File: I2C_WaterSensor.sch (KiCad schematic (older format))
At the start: 18 parts, among them J1 AVR-ISP-6, J8 Conn_01x07, U2 ATmega328P-AU, Y1 16MHz

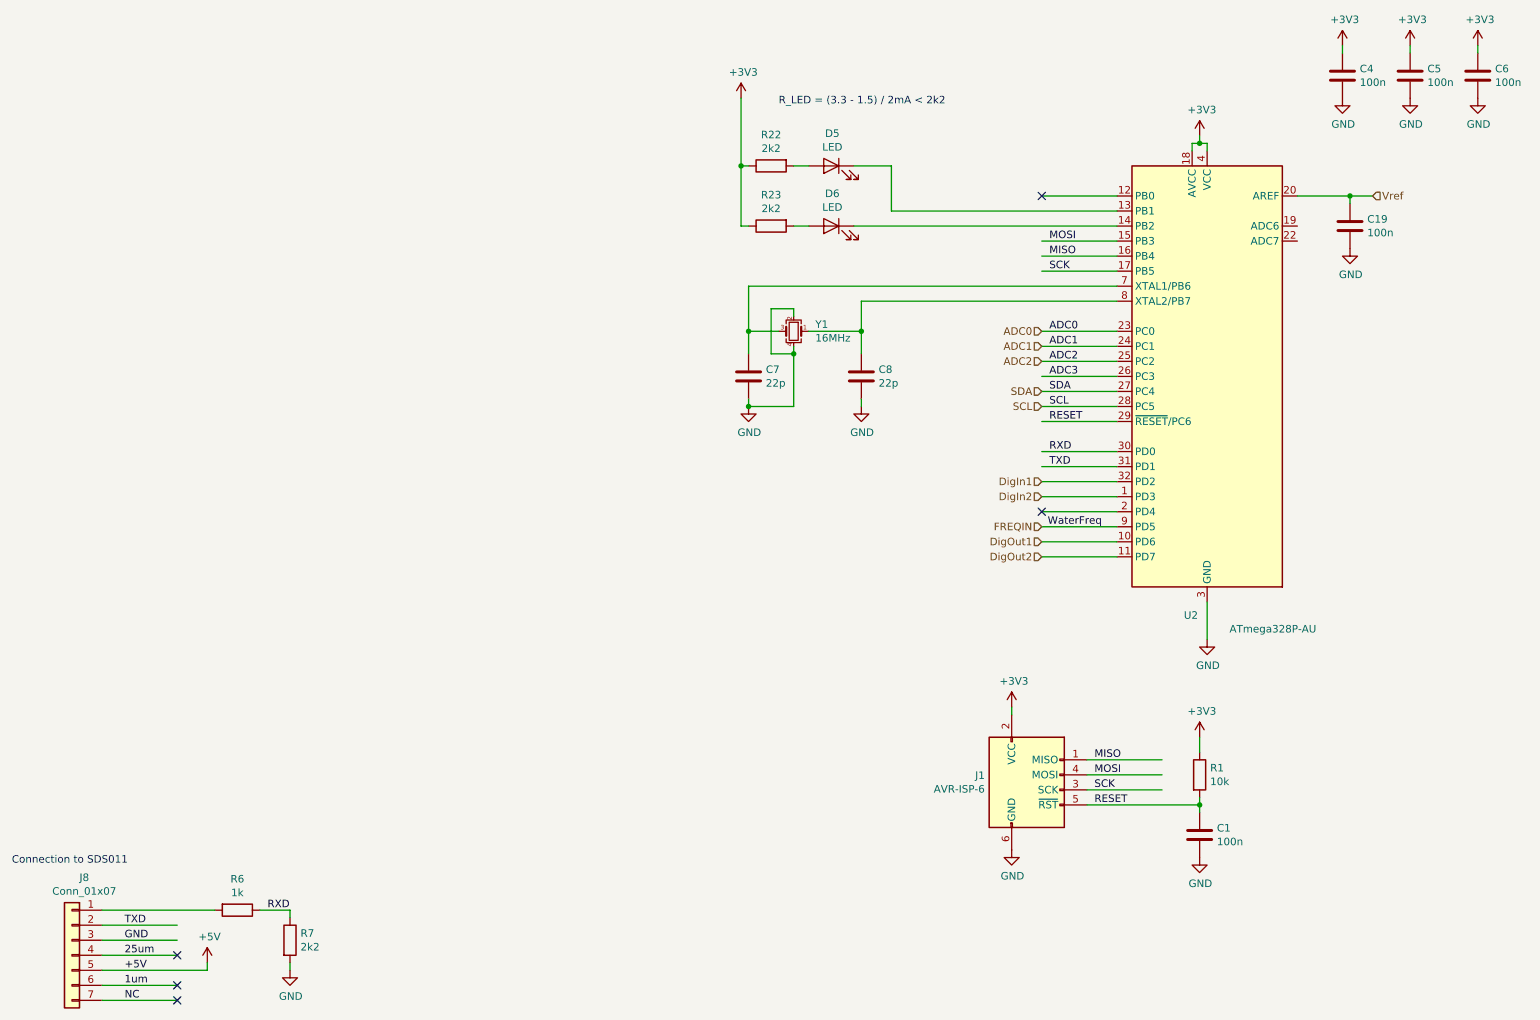
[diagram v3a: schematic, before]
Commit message: included address jumper for AVR, which makes it easier to use multiple of these boards at the same I2C bus.
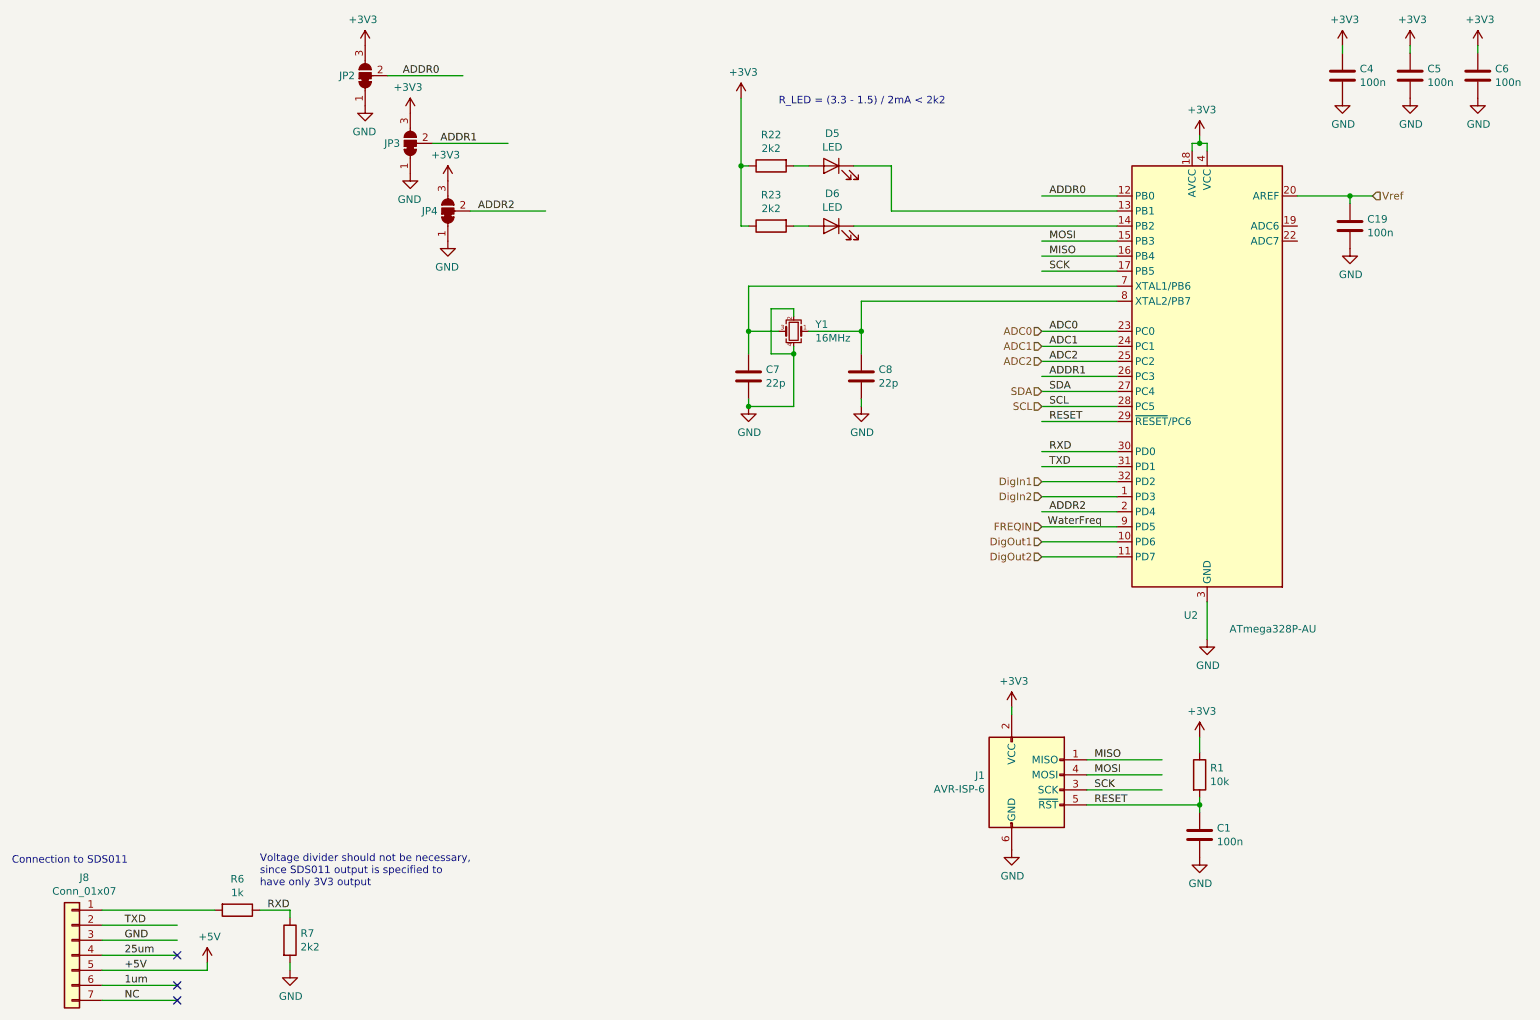
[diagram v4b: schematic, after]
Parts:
- added JP2, JP3, JP4: SolderJumper_3_Bridged12, Jumper:SolderJumper-3_P1.3mm_Bridged12_Pad1.0x1.5mm, symbol Jumper:SolderJumper_3_Bridged12
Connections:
- net labels added: ADDR0, ADDR1, ADDR2
- net labels removed: ADC3
- wire segments 77 -> 80
- no-connect marks 5 -> 3
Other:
- note added: "Voltage divider should not be necessary, \nsince SDS011 output is specified to \nhave only 3V3 output"
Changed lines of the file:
@@
 Text Label 7550 2900 0    50   ~ 0
 ADC2
-Text Label 7550 3000 0    50   ~ 0
-ADC3
 $Comp
 L Connector_Generic:Conn_01x07 J8
@@
 Wire Wire Line
 	1250 6550 2000 6550
-NoConn ~ 7500 3900
-NoConn ~ 7500 1800
 NoConn ~ 1750 7150
 NoConn ~ 1750 7050
@@
 Text HLabel 7500 3800 0    50   Input ~ 0
 DigIn2
+Text Notes 2300 6400 0    50   ~ 0
+Voltage divider should not be necessary, \nsince SDS011 output is specified to \nhave only 3V3 output
+$Comp
+L power:+3V3 #PWR079
+U 1 1 5EEBA048
+P 3000 800
+AR Path="/5E788D14/5EEBA048" Ref="#PWR079"  Part="1"
+AR Path="/5EEBA048" Ref="#PWR?"  Part="1"
+F 0 "#PWR079" H 3000 650 50  0001 C CNN
+F 1 "+3V3" H 3015 973 50  0000 C CNN
+F 2 "" H 3000 800 50  0001 C CNN
+F 3 "" H 3000 800 50  0001 C CNN
+	1    3000 800
+	-1   0    0    -1
+$EndComp
+$Comp
+L power:GND #PWR080
+U 1 1 5EEBA04E
+P 3000 1200
+AR Path="/5E788D14/5EEBA04E" Ref="#PWR080"  Part="1"
+AR Path="/5EEBA04E" Ref="#PWR?"  Part="1"
+F 0 "#PWR080" H 3000 950 50  0001 C CNN
+F 1 "GND" H 3005 1027 50  0000 C CNN
+F 2 "" H 3000 1200 50  0001 C CNN
+F 3 "" H 3000 1200 50  0001 C CNN
+	1    3000 1200
+	-1   0    0    -1
+$EndComp
+$Comp
+L Jumper:SolderJumper_3_Bridged12 JP?
+U 1 1 5EEBA054
+P 3000 1000
+AR Path="/5EEBA054" Ref="JP?"  Part="1"
+AR Path="/5E788D14/5EEBA054" Ref="JP2"  Part="1"
+F 0 "JP2" V 3000 1068 50  0000 L CNN
+F 1 "SolderJumper_3_Bridged12" V 2955 1068 50  0001 L CNN
+F 2 "Jumper:SolderJumper-3_P1.3mm_Bridged12_Pad1.0x1.5mm" H 3000 1000 50  0001 C CNN
+F 3 "~" H 3000 1000 50  0001 C CNN
+	1    3000 1000
+	0    -1   -1   0
+$EndComp
+Wire Wire Line
+	3650 1000 3150 1000
+$Comp
+L power:+3V3 #PWR081
+U 1 1 5EEBCEFD
+P 3300 1250
+AR Path="/5E788D14/5EEBCEFD" Ref="#PWR081"  Part="1"
+AR Path="/5EEBCEFD" Ref="#PWR?"  Part="1"
+F 0 "#PWR081" H 3300 1100 50  0001 C CNN
+F 1 "+3V3" H 3315 1423 50  0000 C CNN
+F 2 "" H 3300 1250 50  0001 C CNN
+F 3 "" H 3300 1250 50  0001 C CNN
+	1    3300 1250
+	-1   0    0    -1
+$EndComp
+$Comp
+L power:GND #PWR082
+U 1 1 5EEBCF03
+P 3300 1650
+AR Path="/5E788D14/5EEBCF03" Ref="#PWR082"  Part="1"
+AR Path="/5EEBCF03" Ref="#PWR?"  Part="1"
+F 0 "#PWR082" H 3300 1400 50  0001 C CNN
+F 1 "GND" H 3305 1477 50  0000 C CNN
+F 2 "" H 3300 1650 50  0001 C CNN
+F 3 "" H 3300 1650 50  0001 C CNN
+	1    3300 1650
+	-1   0    0    -1
+$EndComp
+$Comp
+L Jumper:SolderJumper_3_Bridged12 JP?
+U 1 1 5EEBCF09
+P 3300 1450
+AR Path="/5EEBCF09" Ref="JP?"  Part="1"
+AR Path="/5E788D14/5EEBCF09" Ref="JP3"  Part="1"
+F 0 "JP3" V 3300 1518 50  0000 L CNN
+F 1 "SolderJumper_3_Bridged12" V 3255 1518 50  0001 L CNN
+F 2 "Jumper:SolderJumper-3_P1.3mm_Bridged12_Pad1.0x1.5mm" H 3300 1450 50  0001 C CNN
+F 3 "~" H 3300 1450 50  0001 C CNN
+	1    3300 1450
+	0    -1   -1   0
+$EndComp
+Wire Wire Line
+	3950 1450 3450 1450
+Text Label 3250 1000 0    50   ~ 0
+ADDR0
+Text Label 3500 1450 0    50   ~ 0
+ADDR1
+Text Label 7550 1800 0    50   ~ 0
+ADDR0
+Text Label 7550 3000 0    50   ~ 0
+ADDR1
+Text Label 7550 3900 0    50   ~ 0
+ADDR2
+$Comp
+L power:+3V3 #PWR083
+U 1 1 5EEC110B
+P 3550 1700
+AR Path="/5E788D14/5EEC110B" Ref="#PWR083"  Part="1"
+AR Path="/5EEC110B" Ref="#PWR?"  Part="1"
+F 0 "#PWR083" H 3550 1550 50  0001 C CNN
+F 1 "+3V3" H 3565 1873 50  0000 C CNN
+F 2 "" H 3550 1700 50  0001 C CNN
+F 3 "" H 3550 1700 50  0001 C CNN
+	1    3550 1700
+	-1   0    0    -1
+$EndComp
+$Comp
+L power:GND #PWR084
+U 1 1 5EEC1111
+P 3550 2100
+AR Path="/5E788D14/5EEC1111" Ref="#PWR084"  Part="1"
+AR Path="/5EEC1111" Ref="#PWR?"  Part="1"
+F 0 "#PWR084" H 3550 1850 50  0001 C CNN
+F 1 "GND" H 3555 1927 50  0000 C CNN
+F 2 "" H 3550 2100 50  0001 C CNN
+F 3 "" H 3550 2100 50  0001 C CNN
+	1    3550 2100
+	-1   0    0    -1
+$EndComp
+$Comp
+L Jumper:SolderJumper_3_Bridged12 JP?
+U 1 1 5EEC1117
+P 3550 1900
+AR Path="/5EEC1117" Ref="JP?"  Part="1"
+AR Path="/5E788D14/5EEC1117" Ref="JP4"  Part="1"
+F 0 "JP4" V 3550 1968 50  0000 L CNN
+F 1 "SolderJumper_3_Bridged12" V 3505 1968 50  0001 L CNN
+F 2 "Jumper:SolderJumper-3_P1.3mm_Bridged12_Pad1.0x1.5mm" H 3550 1900 50  0001 C CNN
+F 3 "~" H 3550 1900 50  0001 C CNN
+	1    3550 1900
+	0    -1   -1   0
+$EndComp
+Wire Wire Line
+	4200 1900 3700 1900
+Text Label 3750 1900 0    50   ~ 0
+ADDR2
 $EndSCHEMATC
